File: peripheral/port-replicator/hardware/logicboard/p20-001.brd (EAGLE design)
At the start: 72 x 72 mm, 8 parts, among them J1 DIN5, J2 DIN5, J3 DIN5

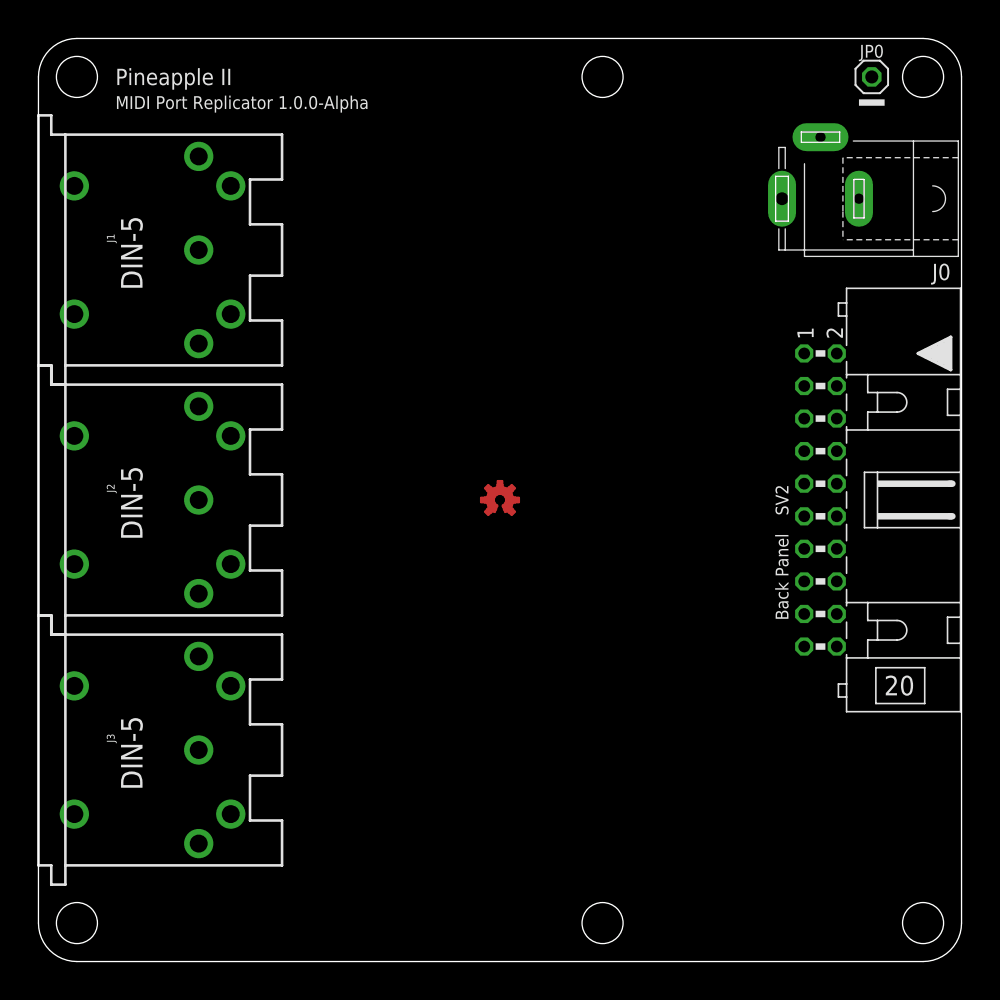
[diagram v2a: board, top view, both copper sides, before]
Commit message: The first artwork for MIDI Port Replicator.
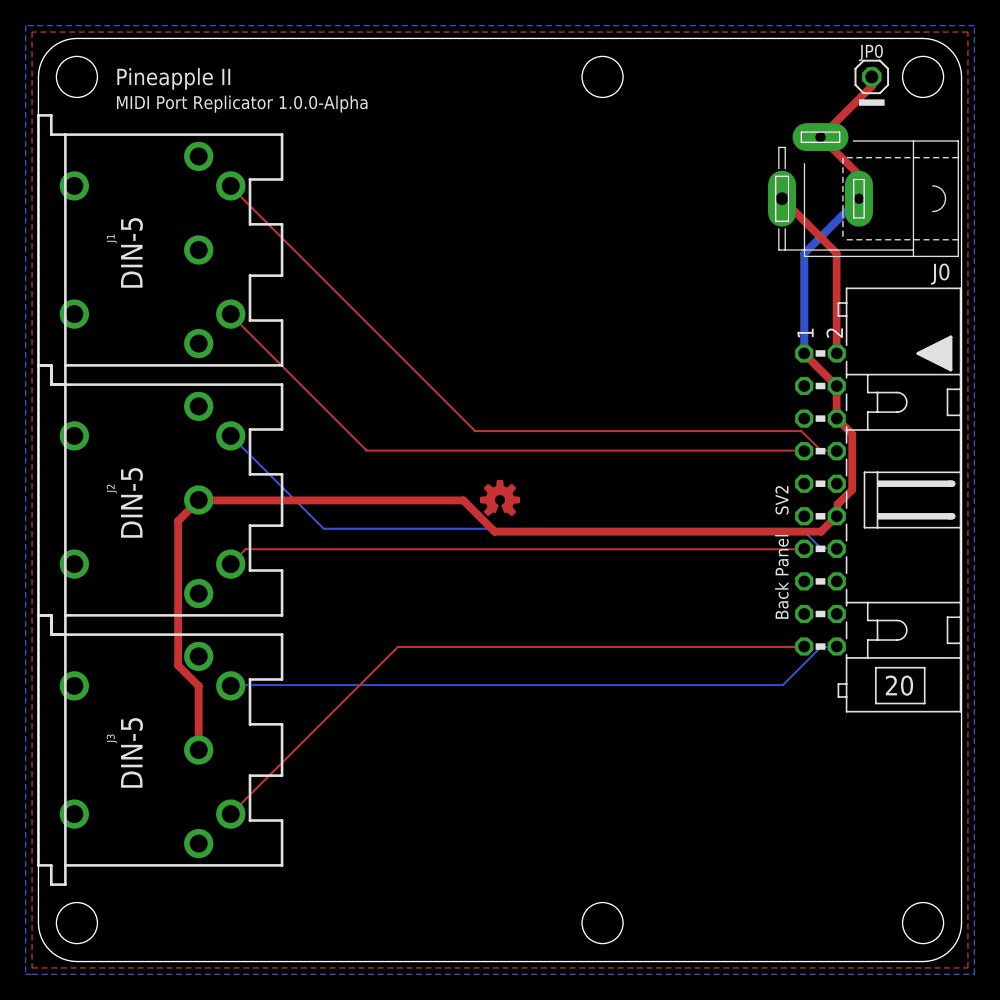
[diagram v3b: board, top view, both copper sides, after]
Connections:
- net GND: now also J0.1, J0.2, J2.2, J3.2
- net MIRETN: now also J1.5
- net MISEND: now also J1.4
- net MO1RETN: now also J2.5
- net MO1SEND: now also J2.4
- net MTRETN: now also J3.5
- net MTSEND: now also J3.4
- net V+: now also J0.3
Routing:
- net GND: track 0.00 -> 113.2 mm
- net MIRETN: track 0.00 -> 55.9 mm
- net MO1RETN: track 0.00 -> 50.9 mm
- net MTSEND: track 0.00 -> 50.1 mm
- net MISEND: track 0.00 -> 49.2 mm
- net MTRETN: track 0.00 -> 48.6 mm
- net MO1SEND: track 0.00 -> 45.2 mm
- net V+: track 0.00 -> 13.8 mm
- added copper zone on layer 1, net GND
- added copper zone on layer 16, net GND
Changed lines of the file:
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@@
 <contactref element="SV2" pad="12"/>
 <contactref element="SV2" pad="1"/>
-<wire x1="59.73" y1="47.43" x2="65" y2="69" width="0" layer="19" extent="1-1"/>
-<wire x1="62.27" y1="44.89" x2="59.73" y2="47.43" width="0" layer="19" extent="1-1"/>
-<wire x1="62.27" y1="42.35" x2="62.27" y2="44.89" width="0" layer="19" extent="1-1"/>
-<wire x1="62.27" y1="34.73" x2="62.27" y2="42.35" width="0" layer="19" extent="1-1"/>
+<contactref element="J2" pad="2"/>
+<contactref element="J3" pad="2"/>
+<contactref element="J0" pad="2"/>
+<contactref element="J0" pad="1"/>
+<wire x1="12.4968" y1="21.4884" x2="12.4968" y2="16.5354" width="0.6096" layer="1"/>
+<wire x1="10.8966" y1="23.0886" x2="12.4968" y2="21.4884" width="0.6096" layer="1"/>
+<wire x1="10.8966" y1="34.3662" x2="10.8966" y2="23.0886" width="0.6096" layer="1"/>
+<wire x1="12.4968" y1="35.9664" x2="10.8966" y2="34.3662" width="0.6096" layer="1"/>
+<wire x1="12.4968" y1="16.5354" x2="12.5" y2="16.5" width="0.6096" layer="1"/>
+<wire x1="12.4968" y1="35.9664" x2="12.5" y2="36" width="0.6096" layer="1"/>
+<wire x1="62.3316" y1="35.6616" x2="62.3316" y2="34.7472" width="0.6096" layer="1"/>
+<wire x1="63.4746" y1="36.8046" x2="62.3316" y2="35.6616" width="0.6096" layer="1"/>
+<wire x1="63.4746" y1="41.148" x2="63.4746" y2="36.8046" width="0.6096" layer="1"/>
+<wire x1="62.3316" y1="42.291" x2="63.4746" y2="41.148" width="0.6096" layer="1"/>
+<wire x1="62.3316" y1="34.7472" x2="62.27" y2="34.73" width="0.6096" layer="1"/>
+<wire x1="62.3316" y1="42.291" x2="62.27" y2="42.35" width="0.6096" layer="1"/>
+<wire x1="62.2554" y1="42.5958" x2="62.2554" y2="44.8818" width="0.6096" layer="1"/>
+<wire x1="62.2554" y1="44.8818" x2="62.27" y2="44.89" width="0.6096" layer="1"/>
+<wire x1="62.2554" y1="42.5958" x2="62.27" y2="42.35" width="0.6096" layer="1"/>
+<wire x1="62.103" y1="45.0342" x2="59.7408" y2="47.3964" width="0.6096" layer="1"/>
+<wire x1="59.7408" y1="47.3964" x2="59.73" y2="47.43" width="0.6096" layer="1"/>
+<wire x1="62.103" y1="45.0342" x2="62.27" y2="44.89" width="0.6096" layer="1"/>
+<wire x1="64.9986" y1="68.2752" x2="64.9986" y2="68.961" width="0.6096" layer="1"/>
+<wire x1="61.0362" y1="64.3128" x2="64.9986" y2="68.2752" width="0.6096" layer="1"/>
+<wire x1="64.9986" y1="68.961" x2="65" y2="69" width="0.6096" layer="1"/>
+<wire x1="61.0362" y1="64.3128" x2="61" y2="64.3" width="0.6096" layer="1"/>
+<wire x1="63.9318" y1="61.4172" x2="63.9318" y2="59.5122" width="0.6096" layer="1"/>
+<wire x1="61.2648" y1="64.0842" x2="63.9318" y2="61.4172" width="0.6096" layer="1"/>
+<wire x1="63.9318" y1="59.5122" x2="64" y2="59.5" width="0.6096" layer="1"/>
+<wire x1="61.2648" y1="64.0842" x2="61" y2="64.3" width="0.6096" layer="1"/>
+<wire x1="59.7408" y1="55.245" x2="59.7408" y2="47.4726" width="0.6096" layer="16"/>
+<wire x1="63.9318" y1="59.436" x2="59.7408" y2="55.245" width="0.6096" layer="16"/>
+<wire x1="59.7408" y1="47.4726" x2="59.73" y2="47.43" width="0.6096" layer="16"/>
+<wire x1="63.9318" y1="59.436" x2="64" y2="59.5" width="0.6096" layer="16"/>
+<wire x1="33.147" y1="35.9664" x2="12.8016" y2="35.9664" width="0.6096" layer="1"/>
+<wire x1="35.5854" y1="33.528" x2="33.147" y2="35.9664" width="0.6096" layer="1"/>
+<wire x1="61.0362" y1="33.528" x2="35.5854" y2="33.528" width="0.6096" layer="1"/>
+<wire x1="62.0268" y1="34.5186" x2="61.0362" y2="33.528" width="0.6096" layer="1"/>
+<wire x1="12.8016" y1="35.9664" x2="12.5" y2="36" width="0.6096" layer="1"/>
+<wire x1="62.0268" y1="34.5186" x2="62.27" y2="34.73" width="0.6096" layer="1"/>
+<polygon width="0.15" layer="1">
+<vertex x="-0.5" y="-0.5"/>
+<vertex x="72.5" y="-0.5"/>
+<vertex x="72.5" y="72.5"/>
+<vertex x="-0.5" y="72.5"/>
+</polygon>
+<polygon width="0.15" layer="16">
+<vertex x="-0.5" y="-1"/>
+<vertex x="73" y="-1"/>
+<vertex x="73" y="73"/>
+<vertex x="-1" y="73"/>
+<vertex x="-1" y="-1"/>
+</polygon>
 </signal>
 <signal name="MTX+">
@@
 <signal name="MISEND">
 <contactref element="SV2" pad="7"/>
+<contactref element="J1" pad="4"/>
+<wire x1="25.6032" y1="39.8526" x2="59.6646" y2="39.8526" width="0.1524" layer="1"/>
+<wire x1="15.0114" y1="50.4444" x2="25.6032" y2="39.8526" width="0.1524" layer="1"/>
+<wire x1="59.6646" y1="39.8526" x2="59.73" y2="39.81" width="0.1524" layer="1"/>
+<wire x1="15.0114" y1="50.4444" x2="15" y2="50.5" width="0.1524" layer="1"/>
 </signal>
 <signal name="MIRETN">
 <contactref element="SV2" pad="8"/>
+<contactref element="J1" pad="5"/>
+<wire x1="61.0362" y1="39.8526" x2="62.2554" y2="39.8526" width="0.1524" layer="1"/>
+<wire x1="59.5122" y1="41.3766" x2="61.0362" y2="39.8526" width="0.1524" layer="1"/>
+<wire x1="34.0614" y1="41.3766" x2="59.5122" y2="41.3766" width="0.1524" layer="1"/>
+<wire x1="15.0114" y1="60.4266" x2="34.0614" y2="41.3766" width="0.1524" layer="1"/>
+<wire x1="62.2554" y1="39.8526" x2="62.27" y2="39.81" width="0.1524" layer="1"/>
+<wire x1="15.0114" y1="60.4266" x2="15" y2="60.5" width="0.1524" layer="1"/>
 </signal>
 <signal name="MTRETN">
 <contactref element="SV2" pad="20"/>
+<contactref element="J3" pad="5"/>
+<wire x1="61.0362" y1="24.5364" x2="62.2554" y2="24.5364" width="0.1524" layer="16"/>
+<wire x1="58.0644" y1="21.5646" x2="61.0362" y2="24.5364" width="0.1524" layer="16"/>
+<wire x1="15.0114" y1="21.5646" x2="58.0644" y2="21.5646" width="0.1524" layer="16"/>
+<wire x1="62.2554" y1="24.5364" x2="62.27" y2="24.57" width="0.1524" layer="16"/>
+<wire x1="15.0114" y1="21.5646" x2="15" y2="21.5" width="0.1524" layer="16"/>
 </signal>
 <signal name="MTSEND">
 <contactref element="SV2" pad="19"/>
+<contactref element="J3" pad="4"/>
+<wire x1="28.0416" y1="24.5364" x2="59.6646" y2="24.5364" width="0.1524" layer="1"/>
+<wire x1="15.0114" y1="11.5062" x2="28.0416" y2="24.5364" width="0.1524" layer="1"/>
+<wire x1="59.6646" y1="24.5364" x2="59.73" y2="24.57" width="0.1524" layer="1"/>
+<wire x1="15.0114" y1="11.5062" x2="15" y2="11.5" width="0.1524" layer="1"/>
 </signal>
 <signal name="MO1RETN">
 <contactref element="SV2" pad="14"/>
+<contactref element="J2" pad="5"/>
+<wire x1="61.0362" y1="32.2326" x2="62.2554" y2="32.2326" width="0.1524" layer="16"/>
+<wire x1="59.5122" y1="33.7566" x2="61.0362" y2="32.2326" width="0.1524" layer="16"/>
+<wire x1="22.2504" y1="33.7566" x2="59.5122" y2="33.7566" width="0.1524" layer="16"/>
+<wire x1="15.0114" y1="40.9956" x2="22.2504" y2="33.7566" width="0.1524" layer="16"/>
+<wire x1="62.2554" y1="32.2326" x2="62.27" y2="32.19" width="0.1524" layer="16"/>
+<wire x1="15.0114" y1="40.9956" x2="15" y2="41" width="0.1524" layer="16"/>
 </signal>
 <signal name="MO1SEND">
 <contactref element="SV2" pad="13"/>
+<contactref element="J2" pad="4"/>
+<wire x1="16.1544" y1="32.1564" x2="59.6646" y2="32.1564" width="0.1524" layer="1"/>
+<wire x1="15.0114" y1="31.0134" x2="16.1544" y2="32.1564" width="0.1524" layer="1"/>
+<wire x1="59.6646" y1="32.1564" x2="59.73" y2="32.19" width="0.1524" layer="1"/>
+<wire x1="15.0114" y1="31.0134" x2="15" y2="31" width="0.1524" layer="1"/>
 </signal>
 <signal name="MO2RETN">
@@
 <signal name="V+" class="2">
 <contactref element="SV2" pad="2"/>
+<contactref element="J0" pad="3"/>
+<wire x1="62.2554" y1="55.245" x2="62.2554" y2="47.4726" width="0.6096" layer="1"/>
+<wire x1="58.0644" y1="59.436" x2="62.2554" y2="55.245" width="0.6096" layer="1"/>
+<wire x1="62.2554" y1="47.4726" x2="62.27" y2="47.43" width="0.6096" layer="1"/>
+<wire x1="58.0644" y1="59.436" x2="58" y2="59.5" width="0.6096" layer="1"/>
 </signal>
 <signal name="LED0A">
